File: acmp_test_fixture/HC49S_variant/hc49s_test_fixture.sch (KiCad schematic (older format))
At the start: 11 parts, among them J1 Conn_Coaxial, J2 Conn_Coaxial, Y1 Crystal

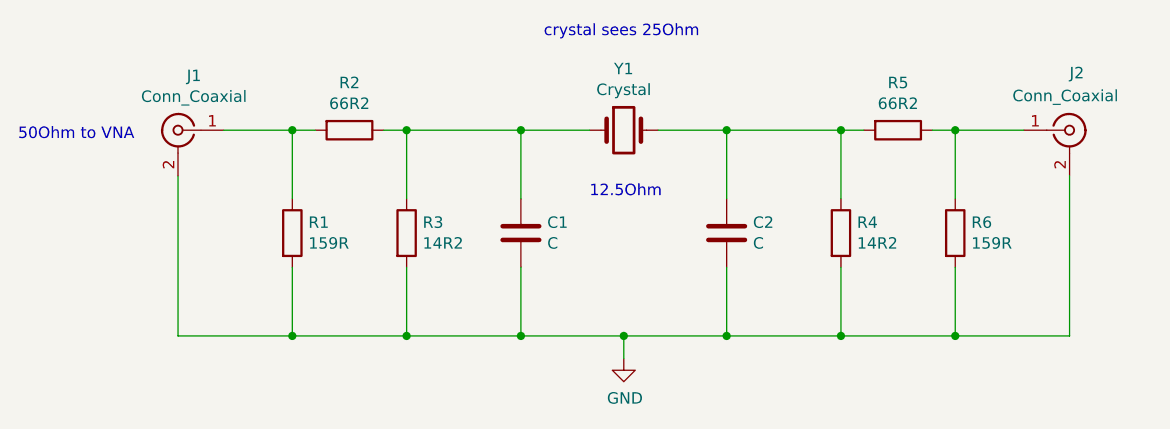
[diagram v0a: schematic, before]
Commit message: added variant of test fixture
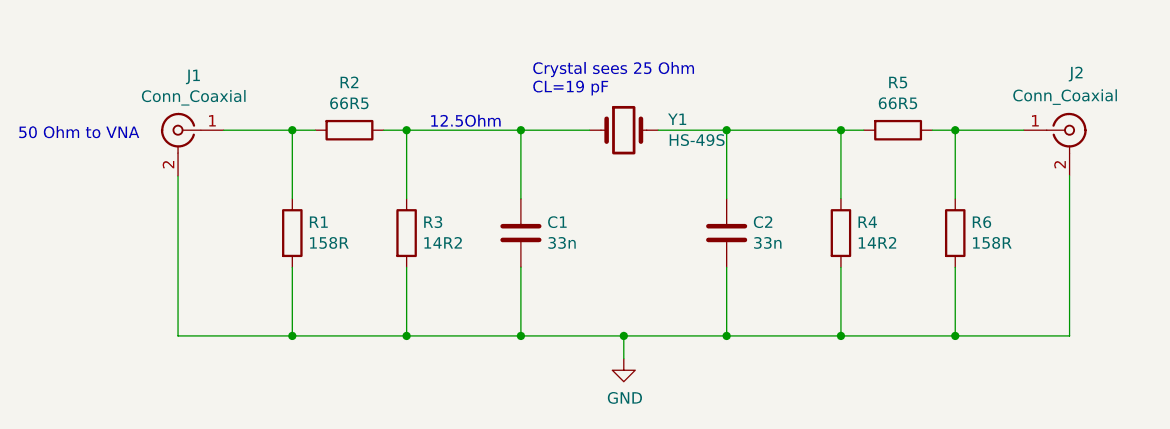
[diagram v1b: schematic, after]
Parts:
- C1, C2: value C -> 33n; footprint (none) -> Capacitor_SMD:C_0603_1608Metric
- J1, J2: footprint (none) -> Connector_Coaxial:SMA_Amphenol_132289_EdgeMount
- R1, R6: value 159R -> 158R; footprint (none) -> Resistor_SMD:R_0603_1608Metric
- R2, R5: value 66R2 -> 66R5; footprint (none) -> Resistor_SMD:R_0603_1608Metric
- R3, R4: footprint (none) -> Resistor_SMD:R_0603_1608Metric
- Y1: value Crystal -> HS-49S; footprint (none) -> Crystal:Crystal_HC49-U_Vertical
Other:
- note added: "50 Ohm to VNA"
- note added: "Crystal sees 25 Ohm\nCL=19 pF"
- note removed: "50Ohm to VNA"
- note removed: "crystal sees 25Ohm"
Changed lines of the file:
@@
 EESchema Schematic File Version 4
-EELAYER 26 0
+EELAYER 30 0
 EELAYER END
 $Descr A4 11693 8268
@@
 P 7600 3950
 F 0 "R6" H 7670 3996 50  0000 L CNN
-F 1 "159R" H 7670 3905 50  0000 L CNN
-F 2 "" V 7530 3950 50  0001 C CNN
+F 1 "158R" H 7670 3905 50  0000 L CNN
+F 2 "Resistor_SMD:R_0603_1608Metric" V 7530 3950 50  0001 C CNN
 F 3 "~" H 7600 3950 50  0001 C CNN
 	1    7600 3950
@@
 F 0 "R4" H 7170 3996 50  0000 L CNN
 F 1 "14R2" H 7170 3905 50  0000 L CNN
-F 2 "" V 7030 3950 50  0001 C CNN
+F 2 "Resistor_SMD:R_0603_1608Metric" V 7030 3950 50  0001 C CNN
 F 3 "~" H 7100 3950 50  0001 C CNN
 	1    7100 3950
@@
 P 7350 3500
 F 0 "R5" V 7143 3500 50  0000 C CNN
-F 1 "66R2" V 7234 3500 50  0000 C CNN
-F 2 "" V 7280 3500 50  0001 C CNN
+F 1 "66R5" V 7234 3500 50  0000 C CNN
+F 2 "Resistor_SMD:R_0603_1608Metric" V 7280 3500 50  0001 C CNN
 F 3 "~" H 7350 3500 50  0001 C CNN
 	1    7350 3500
@@
 F 0 "R3" H 5270 3996 50  0000 L CNN
 F 1 "14R2" H 5270 3905 50  0000 L CNN
-F 2 "" V 5130 3950 50  0001 C CNN
+F 2 "Resistor_SMD:R_0603_1608Metric" V 5130 3950 50  0001 C CNN
 F 3 "~" H 5200 3950 50  0001 C CNN
 	1    5200 3950
@@
 P 4700 3950
 F 0 "R1" H 4770 3996 50  0000 L CNN
-F 1 "159R" H 4770 3905 50  0000 L CNN
-F 2 "" V 4630 3950 50  0001 C CNN
+F 1 "158R" H 4770 3905 50  0000 L CNN
+F 2 "Resistor_SMD:R_0603_1608Metric" V 4630 3950 50  0001 C CNN
 F 3 "~" H 4700 3950 50  0001 C CNN
 	1    4700 3950
@@
 P 4950 3500
 F 0 "R2" V 4743 3500 50  0000 C CNN
-F 1 "66R2" V 4834 3500 50  0000 C CNN
-F 2 "" V 4880 3500 50  0001 C CNN
+F 1 "66R5" V 4834 3500 50  0000 C CNN
+F 2 "Resistor_SMD:R_0603_1608Metric" V 4880 3500 50  0001 C CNN
 F 3 "~" H 4950 3500 50  0001 C CNN
 	1    4950 3500
@@
 P 5700 3950
 F 0 "C1" H 5815 3996 50  0000 L CNN
-F 1 "C" H 5815 3905 50  0000 L CNN
-F 2 "" H 5738 3800 50  0001 C CNN
+F 1 "33n" H 5815 3905 50  0000 L CNN
+F 2 "Capacitor_SMD:C_0603_1608Metric" H 5738 3800 50  0001 C CNN
 F 3 "~" H 5700 3950 50  0001 C CNN
 	1    5700 3950
@@
 P 6600 3950
 F 0 "C2" H 6715 3996 50  0000 L CNN
-F 1 "C" H 6715 3905 50  0000 L CNN
-F 2 "" H 6638 3800 50  0001 C CNN
+F 1 "33n" H 6715 3905 50  0000 L CNN
+F 2 "Capacitor_SMD:C_0603_1608Metric" H 6638 3800 50  0001 C CNN
 F 3 "~" H 6600 3950 50  0001 C CNN
 	1    6600 3950
-	1    0    0    -1
-$EndComp
-$Comp
-L Device:Crystal Y1
-U 1 1 5D613084
-P 6150 3500
-F 0 "Y1" H 6150 3768 50  0000 C CNN
-F 1 "Crystal" H 6150 3677 50  0000 C CNN
-F 2 "" H 6150 3500 50  0001 C CNN
-F 3 "~" H 6150 3500 50  0001 C CNN
-	1    6150 3500
 	1    0    0    -1
 $EndComp
@@
 F 0 "J2" H 8100 3750 50  0000 L CNN
 F 1 "Conn_Coaxial" H 7850 3650 50  0000 L CNN
-F 2 "" H 8100 3500 50  0001 C CNN
+F 2 "Connector_Coaxial:SMA_Amphenol_132289_EdgeMount" H 8100 3500 50  0001 C CNN
 F 3 " ~" H 8100 3500 50  0001 C CNN
 	1    8100 3500
@@
 F 0 "J1" H 4130 3738 50  0000 C CNN
 F 1 "Conn_Coaxial" H 4130 3647 50  0000 C CNN
-F 2 "" H 4200 3500 50  0001 C CNN
+F 2 "Connector_Coaxial:SMA_Amphenol_132289_EdgeMount" H 4200 3500 50  0001 C CNN
 F 3 " ~" H 4200 3500 50  0001 C CNN
 	1    4200 3500
@@
 Wire Wire Line
 	6150 4500 6150 4400
+Wire Wire Line
+	6150 4400 6600 4400
+Text Notes 5750 3350 0    50   ~ 0
+Crystal sees 25 Ohm\nCL=19 pF
+Text Notes 3500 3550 0    50   ~ 0
+50 Ohm to VNA
+Text Notes 5300 3500 0    50   ~ 0
+12.5Ohm
 Connection ~ 6150 4400
-Wire Wire Line
-	6150 4400 6600 4400
-Text Notes 5800 3100 0    50   ~ 0
-crystal sees 25Ohm
-Text Notes 3500 3550 0    50   ~ 0
-50Ohm to VNA
-Text Notes 6000 3800 0    50   ~ 0
-12.5Ohm
+$Comp
+L Device:Crystal Y1
+U 1 1 5DDDC3CC
+P 6150 3500
+F 0 "Y1" H 6344 3546 50  0000 L CNN
+F 1 "HS-49S" H 6344 3455 50  0000 L CNN
+F 2 "Crystal:Crystal_HC49-U_Vertical" H 6150 3500 50  0001 C CNN
+F 3 "~" H 6150 3500 50  0001 C CNN
+	1    6150 3500
+	1    0    0    -1
+$EndComp
 $EndSCHEMATC
